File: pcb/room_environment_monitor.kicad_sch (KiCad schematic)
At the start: 43 parts, among them J1 Conn_01x02_Pin, J2 Conn_01x04_Pin, P1 USB_C_Plug_USB2.0, Q1 BSS138, Q2 BSS138, Q3 BSS138, SW1 SW_SPST, SW3 SW_SPST, U1 D1213A-04V, U2 ESP32-C3-MINI-1, U3 BME280, U4 SGP30-2.5K, U5 AP2127N-1.8, U7 AZ1117-3.3

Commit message: get the schematic done, need to optomize for parts
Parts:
- removed C4, C5, C8, C9: 100n, symbol Device:C_Small
- removed D3, D4, D5, D6: SK6805, LED_SMD:LED_SK6805_PLCC4_2.4x2.7mm_P1.3mm, symbol LED:SK6805
- removed J2: Conn_01x04_Pin, Connector_JST:JST_ZE_BM04B-ZESS-TBT_1x04-1MP_P1.50mm_Vertical, symbol Connector:Conn_01x04_Pin
- removed Q1, Q2: BSS138, Package_TO_SOT_SMD:SOT-23, symbol Transistor_FET:BSS138
- removed R4, R5, R6, R7, R8: 10k, symbol Device:R_Small_US
- removed SW3: SW_SPST, Button_Switch_SMD:SW_Push_1P1T_NO_CK_KMR2, symbol Switch:SW_SPST
- removed TP2, TP3: TestPoint, TestPoint:TestPoint_Pad_D1.0mm, symbol Connector:TestPoint
- removed U3: BME280, Package_LGA:Bosch_LGA-8_2.5x2.5mm_P0.65mm_ClockwisePinNumbering, symbol Sensor:BME280
- removed U4: SGP30-2.5K, Kevin_Lutzer_Lbr:SGP30-2.5K_SEN-M, symbol Kevin_Lutzer_Lbr:SGP30-2.5K
- added C12, C14: 10u, Capacitor_SMD:C_0603_1608Metric, symbol Device:C_Small
- added C13: 1u, Capacitor_SMD:C_0603_1608Metric, symbol Device:C_Small
- added D3, D4, D5: SK6812MINI, LED_SMD:LED_SK6812MINI_PLCC4_3.5x3.5mm_P1.75mm, symbol LED:SK6812MINI
- added D7, D8: LED, LED_SMD:LED_0603_1608Metric, symbol Device:LED
- added Q6, Q7: BSS138, Package_TO_SOT_SMD:SOT-23, symbol Transistor_FET:BSS138
- added R12, R21: 10k, Resistor_SMD:R_0603_1608Metric, symbol Device:R_Small_US
- added R13: NC, Resistor_SMD:R_0603_1608Metric, symbol Device:R_Small_US
- added R14: 22.1k, Resistor_SMD:R_0603_1608Metric, symbol Device:R_Small_US
- added R15: 47.5k, Resistor_SMD:R_0603_1608Metric, symbol Device:R_Small_US
- added R16, R17: 0, Resistor_SMD:R_0603_1608Metric, symbol Device:R_Small_US
- added R18, R19: 220, Resistor_SMD:R_0603_1608Metric, symbol Device:R_Small_US
- added R20: 5.1k, Resistor_SMD:R_0603_1608Metric, symbol Device:R_Small_US
- added SW2: SW_SPST, Button_Switch_SMD:SW_Push_1P1T_NO_CK_KMR2, symbol Switch:SW_SPST
- added U8: CP2102N-Axx-xQFN28, Package_DFN_QFN:QFN-28-1EP_5x5mm_P0.5mm_EP3.35x3.35mm, symbol Interface_USB:CP2102N-Axx-xQFN28
- C1, C10, C11, C3, C6, C7: footprint (none) -> Capacitor_SMD:C_0603_1608Metric
- C2: value 10u -> 100n; footprint (none) -> Capacitor_SMD:C_0603_1608Metric
- D2: footprint (none) -> LED_SMD:LED_0603_1608Metric
- R1: footprint (none) -> Resistor_SMD:R_0603_1608Metric
- R2: value 10k -> 220; footprint (none) -> Resistor_SMD:R_0603_1608Metric
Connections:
- net +3V3: now also D3.4 (VDD), D4.4 (VDD), D5.4 (VDD), R21.1; no longer C2.1
- net +5V: now also C12.1, C14.1, R12.1, R14.1, U8.6 (VDD), U8.7 (VREGIN); no longer U2.30 (GPIO20/U0RXD), U2.31 (GPIO21/U0TXD)
- net BOOT: now also C2.1, U2.23 (GPIO9), Q7.3 (D), R21.2, SW2.2 (B); no longer U2.22 (GPIO8)
- net EN: now also Q6.3 (D)
- net GND: now also C12.2, C13.2, C14.2, D3.2 (VSS), D4.2 (VSS), D5.2 (VSS), D7.1 (K), D8.1 (K), R13.2, R15.1, R20.2, SW2.1 (A), U8.29 (GND), U8.3 (GND)
- net NEOPIXEL: now also U2.22 (GPIO8), D3.3 (DIN); no longer U2.23 (GPIO9)
- net USB_D+: now also U8.4 (D+); no longer U2.27 (GPIO19/USB_D+)
- net USB_D-: now also U8.5 (D-); no longer U2.26 (GPIO18/USB_D-)
- net CC: now reaches P1.A5 (CC)
- net CC: now also R20.1
- net UART1_RX: now reaches U2.18 (GPIO4/ADC1_CH4)
- net UART1_TX: now reaches U2.19 (GPIO5/ADC2_CH0)
- new net: R13.1, U8.11 (~{SUSPEND})
- new net: D4.1 (DOUT), D5.3 (DIN)
- new net: D3.1 (DOUT), D4.3 (DIN)
- new net: D8.2 (A), R19.1
- new net: D7.2 (A), R18.1
- new net: C13.1, R14.2, R15.2, U8.8 (VBUS)
- new net: R17.1, U8.25 (RXD)
- new net: R16.1, U8.26 (TXD)
- new net: R12.2, U8.9 (~{RST})
- new net DTR: Q6.1 (G), Q7.2 (S), U8.28 (~{DTR})
- new net RTS: Q6.2 (S), Q7.1 (G), U8.24 (~{RTS})
- new net RX_LED: R19.2, U8.15 (CHR0)
- new net TX_LED: R18.2, U8.14 (CHR1)
- new net UART_RX: R16.2, U2.30 (GPIO20/U0RXD)
- new net UART_TX: R17.2, U2.31 (GPIO21/U0TXD)
- no-connect marks 7 -> 8
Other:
- added sheet Sensors (sensors.kicad_sch)
- note added: "CC Resistor might have to be 10.2k"
- note added: "ESP32"
- note added: "USB/UART"
- note removed: "4 Pin Connector Is for PM1006"
- note removed: "Address 0x77"
- note removed: "Check to make sure CC and VCONN are connected properly"
- note removed: "SGP30 Level Shifter"
- note removed: "Sensors (BME280, PM1006, SGP30)"
- note removed: "Verify this."
- moved on the sheet: C1, C3, D1, J1, Q3, R1, SW1, TP1, U2

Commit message: WIP
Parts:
- removed C6, C7: 1u, Capacitor_SMD:C_0603_1608Metric, symbol Device:C_Small
- removed TP5: TestPoint, TestPoint:TestPoint_Pad_D1.0mm, symbol Connector:TestPoint
- removed U5: AP2127N-1.8, Package_TO_SOT_SMD:SOT-23, symbol Regulator_Linear:AP2127N-1.8
- P1: footprint (none) -> Kevin_Lutzer_Lbr:CONN6_USB4130-GF-C_GCT
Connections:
- net FAN-: no longer names the net of D1.2 (A), J1.2 (Pin_2), Q3.3 (D), TP1.1
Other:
- moved on the sheet: D2, R2

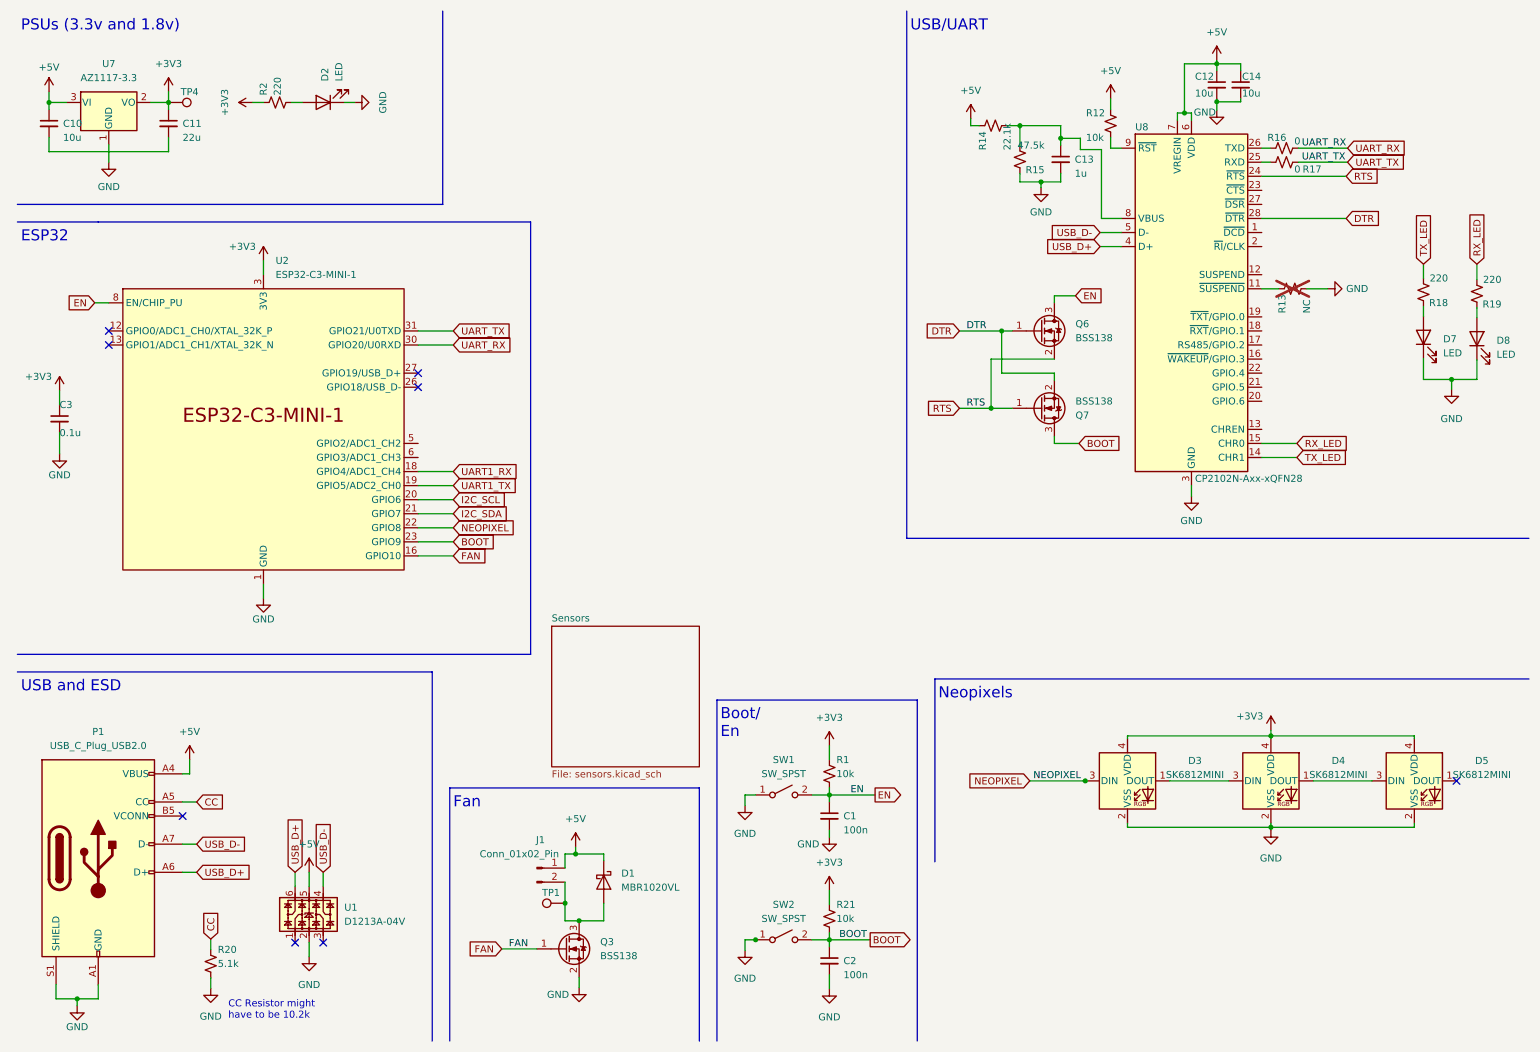
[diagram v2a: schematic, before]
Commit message: finish the routing need to move the esp32 up 5.5 mm
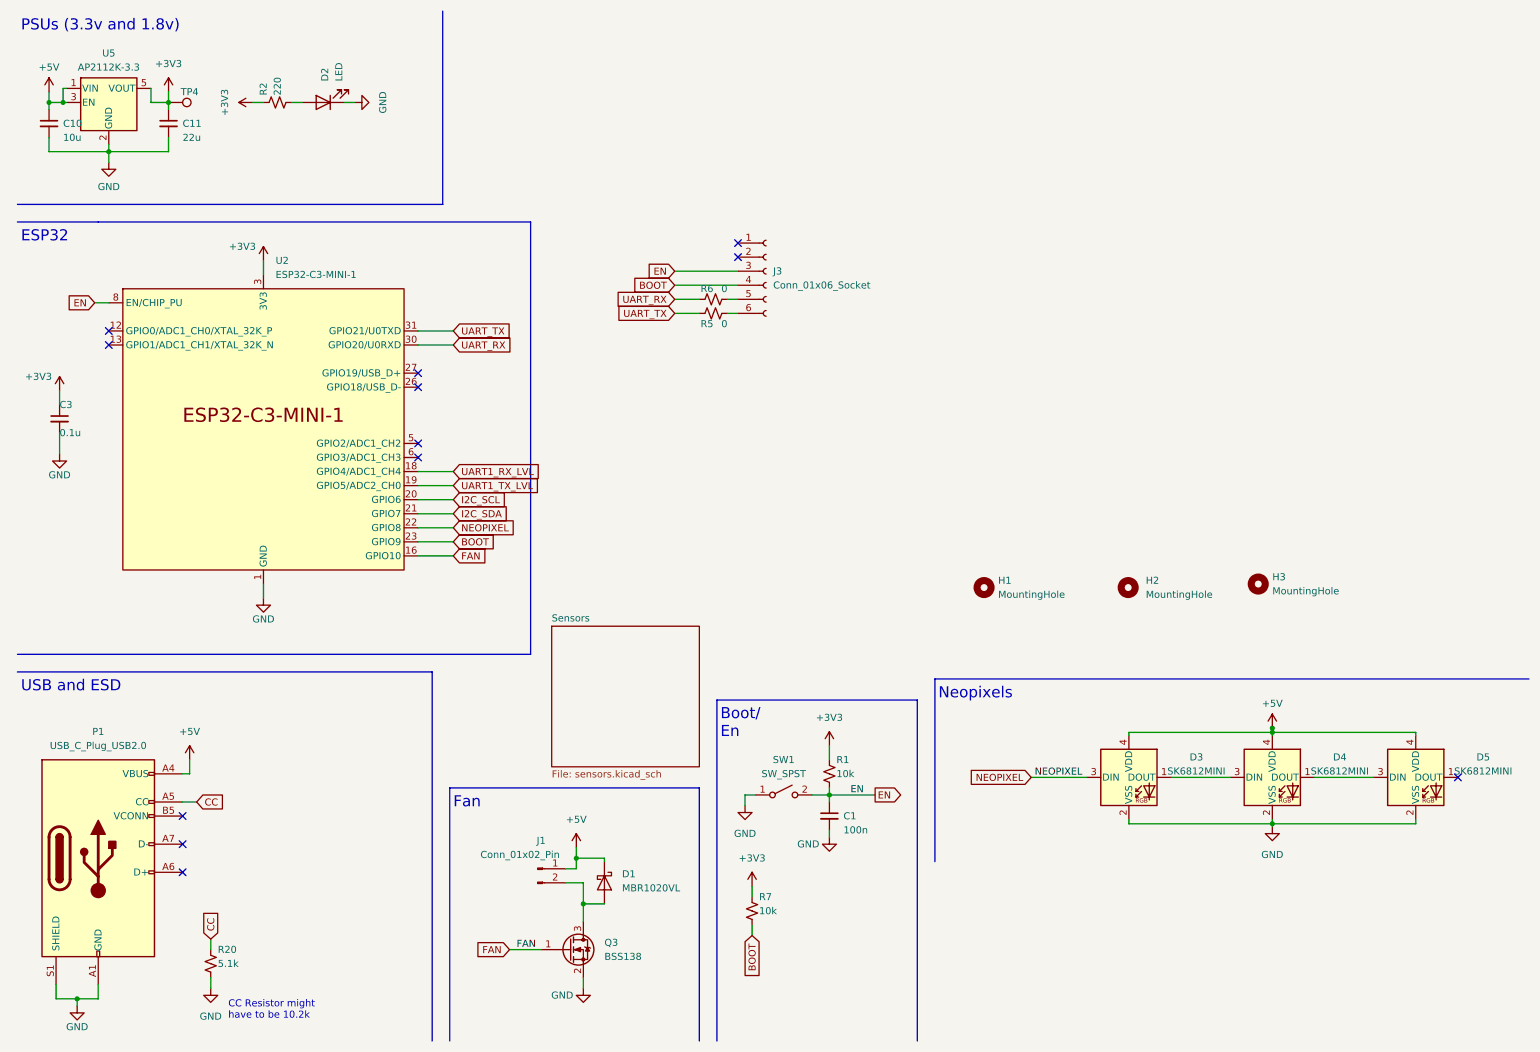
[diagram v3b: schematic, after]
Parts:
- removed C12, C14: 10u, Capacitor_SMD:C_0603_1608Metric, symbol Device:C_Small
- removed C13: 1u, Capacitor_SMD:C_0603_1608Metric, symbol Device:C_Small
- removed C2: 100n, Capacitor_SMD:C_0603_1608Metric, symbol Device:C_Small
- removed D7, D8: LED, LED_SMD:LED_0603_1608Metric, symbol Device:LED
- removed Q6, Q7: BSS138, Package_TO_SOT_SMD:SOT-23, symbol Transistor_FET:BSS138
- removed R12, R21: 10k, Resistor_SMD:R_0603_1608Metric, symbol Device:R_Small_US
- removed R13: NC, Resistor_SMD:R_0603_1608Metric, symbol Device:R_Small_US
- removed R14: 22.1k, Resistor_SMD:R_0603_1608Metric, symbol Device:R_Small_US
- removed R15: 47.5k, Resistor_SMD:R_0603_1608Metric, symbol Device:R_Small_US
- removed R16, R17: 0, Resistor_SMD:R_0603_1608Metric, symbol Device:R_Small_US
- removed R18, R19: 220, Resistor_SMD:R_0603_1608Metric, symbol Device:R_Small_US
- removed SW2: SW_SPST, Button_Switch_SMD:SW_Push_1P1T_NO_CK_KMR2, symbol Switch:SW_SPST
- removed TP1: TestPoint, TestPoint:TestPoint_Pad_D1.0mm, symbol Connector:TestPoint
- removed U1: D1213A-04V, Package_TO_SOT_SMD:SOT-363_SC-70-6, symbol Kevin_Lutzer_Lbr:D1213A-04V
- removed U7: AZ1117-3.3, Package_TO_SOT_SMD:SOT-23-5, symbol Regulator_Linear:AZ1117-3.3
- removed U8: CP2102N-Axx-xQFN28, Package_DFN_QFN:QFN-28-1EP_5x5mm_P0.5mm_EP3.35x3.35mm, symbol Interface_USB:CP2102N-Axx-xQFN28
- added H1, H2, H3: MountingHole, MountingHole:MountingHole_2.2mm_M2_DIN965, symbol Mechanical:MountingHole
- added J3: Conn_01x06_Socket, Connector_JST:JST_GH_SM06B-GHS-TB_1x06-1MP_P1.25mm_Horizontal, symbol Connector:Conn_01x06_Socket
- added R5, R6: 0, Resistor_SMD:R_0603_1608Metric, symbol Device:R_Small_US
- added R7: 10k, Resistor_SMD:R_0603_1608Metric, symbol Device:R_Small_US
- added U5: AP2112K-3.3, Package_TO_SOT_SMD:SOT-23-5, symbol Regulator_Linear:AP2112K-3.3
- J1: footprint Connector_JST:JST_GH_BM02B-GHS-TBT_1x02-1MP_P1.25mm_Vertical -> Connector_Molex:Molex_CLIK-Mate_502382-0270_1x02-1MP_P1.25mm_Vertical
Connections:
- net +3V3: now also R7.1, U5.5 (VOUT); no longer D3.4 (VDD), D4.4 (VDD), D5.4 (VDD)
- net +5V: now also D3.4 (VDD), D4.4 (VDD), D5.4 (VDD), U5.1 (VIN), U5.3 (EN)
- net BOOT: now also J3.4 (Pin_4), R7.2
- net EN: now also J3.3 (Pin_3)
- net GND: now also C10.2, C11.2, U5.2 (GND)
- net UART_RX: now also R6.1
- net UART_TX: now also R5.1
- net UART1_RX renamed UART1_RX_LVL
- net UART1_TX renamed UART1_TX_LVL
- net USB_D+: no longer names the net of P1.A6 (D+)
- net USB_D-: no longer names the net of P1.A7 (D-)
- new net: J3.6 (Pin_6), R5.2
- new net: J3.5 (Pin_5), R6.2
- no-connect marks 8 -> 12
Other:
- note removed: "USB/UART"
- moved on the sheet: D3, D4, D5, Q3

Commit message: finish routing the PCB
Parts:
- removed SW1: SW_SPST, Button_Switch_SMD:SW_Push_1P1T_NO_CK_KMR2, symbol Switch:SW_SPST
- J1: footprint Connector_Molex:Molex_CLIK-Mate_502382-0270_1x02-1MP_P1.25mm_Vertical -> Connector_Molex:Molex_PicoBlade_53398-0271_1x02-1MP_P1.25mm_Vertical
- J3: footprint Connector_JST:JST_GH_SM06B-GHS-TB_1x06-1MP_P1.25mm_Horizontal -> Connector_JST:JST_SH_SM06B-SRSS-TB_1x06-1MP_P1.00mm_Horizontal
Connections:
- net +5V: now also J1.2 (Pin_2), J3.1 (Pin_1); no longer J1.1 (Pin_1)
- net GND: now also J3.2 (Pin_2)
- net at D1.2 (A), Q3.3 (D): now also J1.1 (Pin_1); no longer J1.2 (Pin_2)
- no-connect marks 12 -> 10
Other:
- moved on the sheet: D3, D4, D5, H1, H2, H3, J3, R5, R6

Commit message: finish v4 and the images for doucmentation
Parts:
- added SW1: SW_SPST, Button_Switch_SMD:SW_Push_1P1T_NO_CK_KMR2, symbol Switch:SW_SPST
- added TP1: TestPoint, TestPoint:TestPoint_Pad_D1.0mm, symbol Connector:TestPoint
- C1: value 100n -> 0u1
- C3: value 0.1u -> 0u1
- D1: value MBR1020VL -> CDBMS160
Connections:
- net EN: now also SW1.2 (B)
- net FAN: now also TP1.1
- net GND: now also SW1.1 (A)
- net PD: now reaches U2.6 (GPIO3/ADC1_CH3)
- net UART1_RX_LVL renamed UART1_RX
- no-connect marks 10 -> 9
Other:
- note added: "Programming Header"
- moved on the sheet: H1, H2, H3, J3, R5, R6

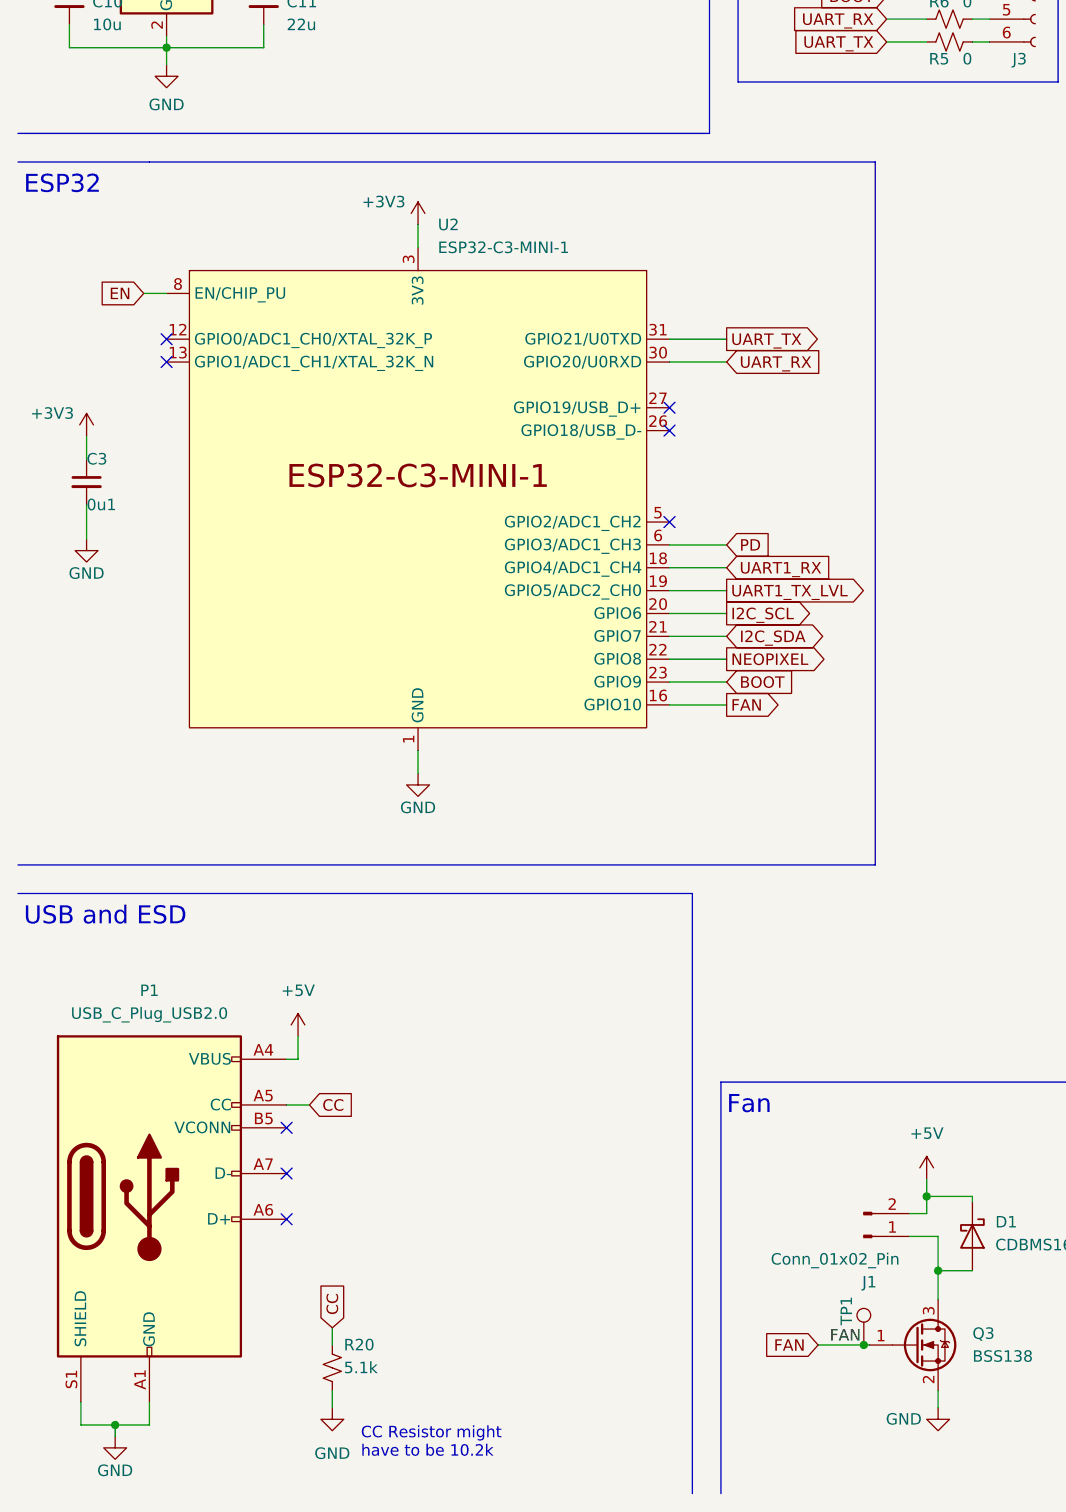
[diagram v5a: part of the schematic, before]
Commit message: cleanup undeeded pdf files and add gerbers
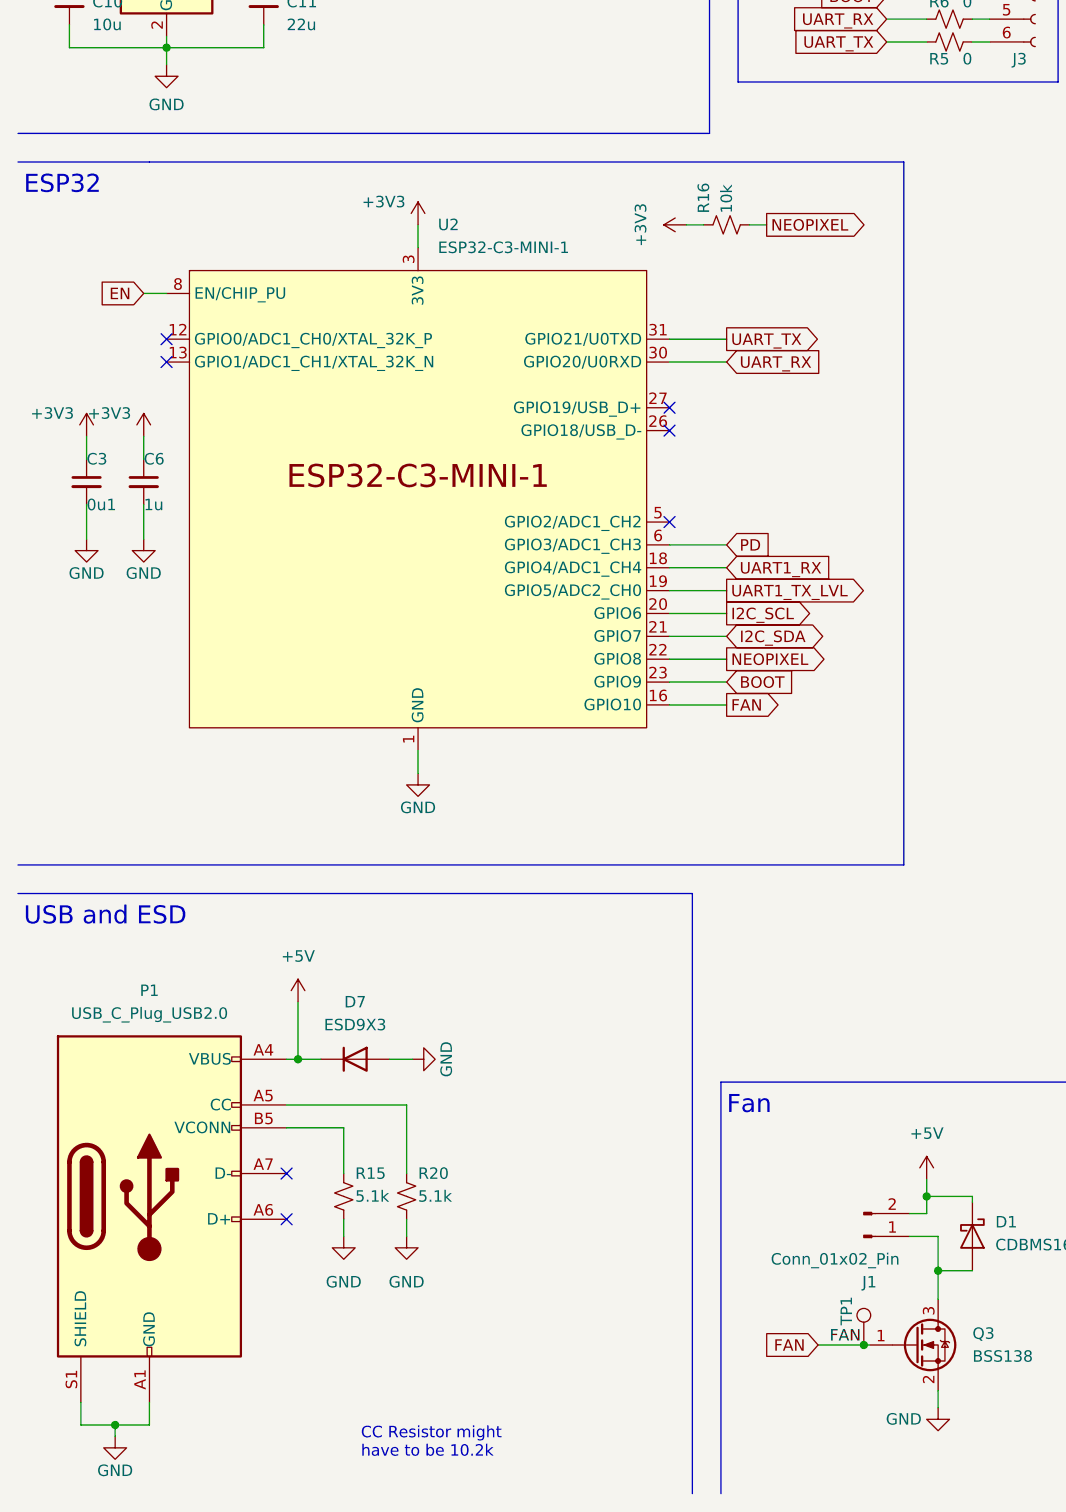
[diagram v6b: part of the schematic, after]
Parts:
- added C6: 1u, Capacitor_SMD:C_0603_1608Metric, symbol Device:C_Small
- added D7: ESD9X3, Diode_SMD:D_SOD-923, symbol Kevin_Lutzer_Lbr:ESD9X5
- added R15: 5.1k, Resistor_SMD:R_0603_1608Metric, symbol Device:R_Small_US
- added R16: 10k, Resistor_SMD:R_0603_1608Metric, symbol Device:R_Small_US
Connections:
- net +3V3: now also C6.1, R16.1
- net +5V: now also D7.1 (K)
- net GND: now also C6.2, D7.2 (A), R15.2
- net NEOPIXEL: now also R16.2
- net at P1.B5 (VCONN): now also R15.1
- net CC: no longer names the net of P1.A5 (CC), R20.1
- no-connect marks 9 -> 8
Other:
- moved on the sheet: R20
